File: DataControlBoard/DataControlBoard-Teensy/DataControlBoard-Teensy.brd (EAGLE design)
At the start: 63.5 x 91.4 mm, 11 parts, among them IC1 74LS165D, IC2 74LS165D, J1 RS-Interface, J2 Pwr-Conn, U1 MAX3232, U2 3V3REG

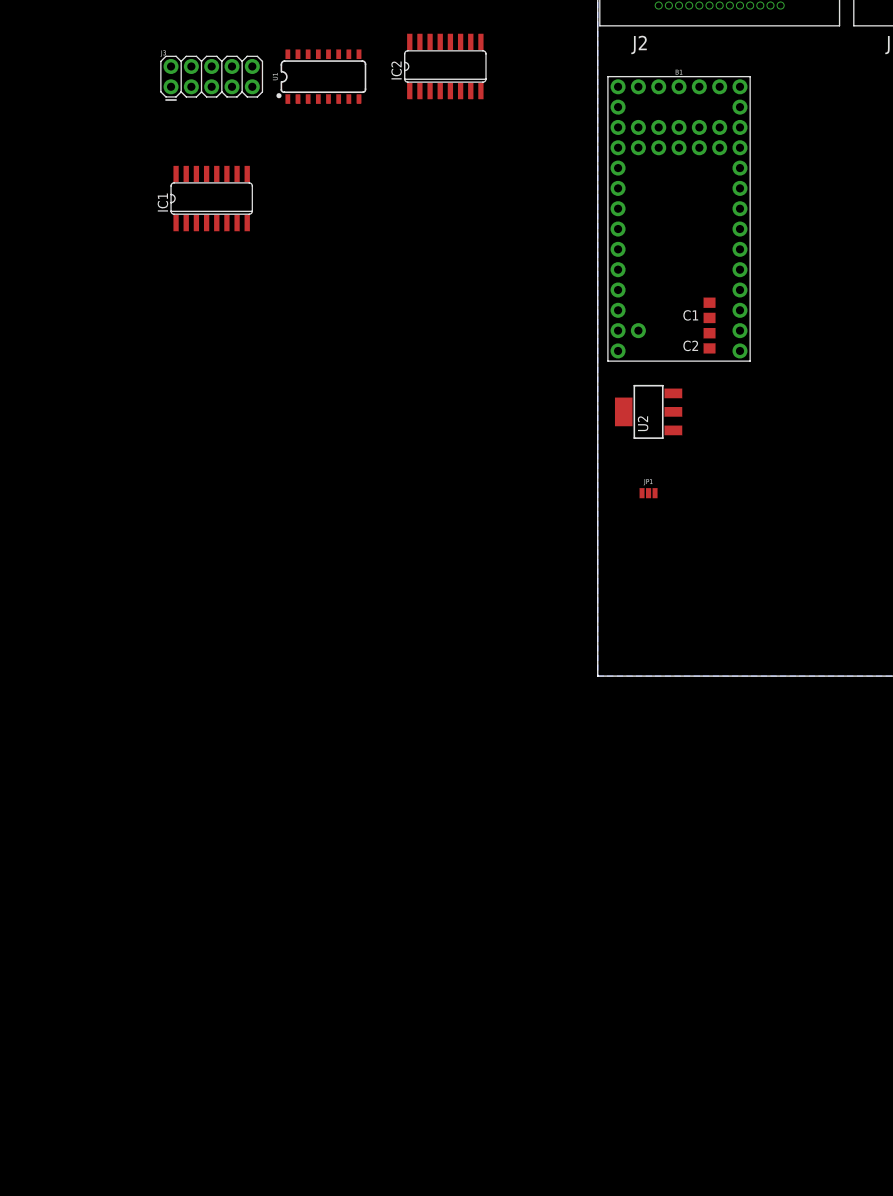
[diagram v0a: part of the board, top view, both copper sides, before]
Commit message: Schematic mostly done. Needs rpi backplane mating header, and a bunch of jumpers
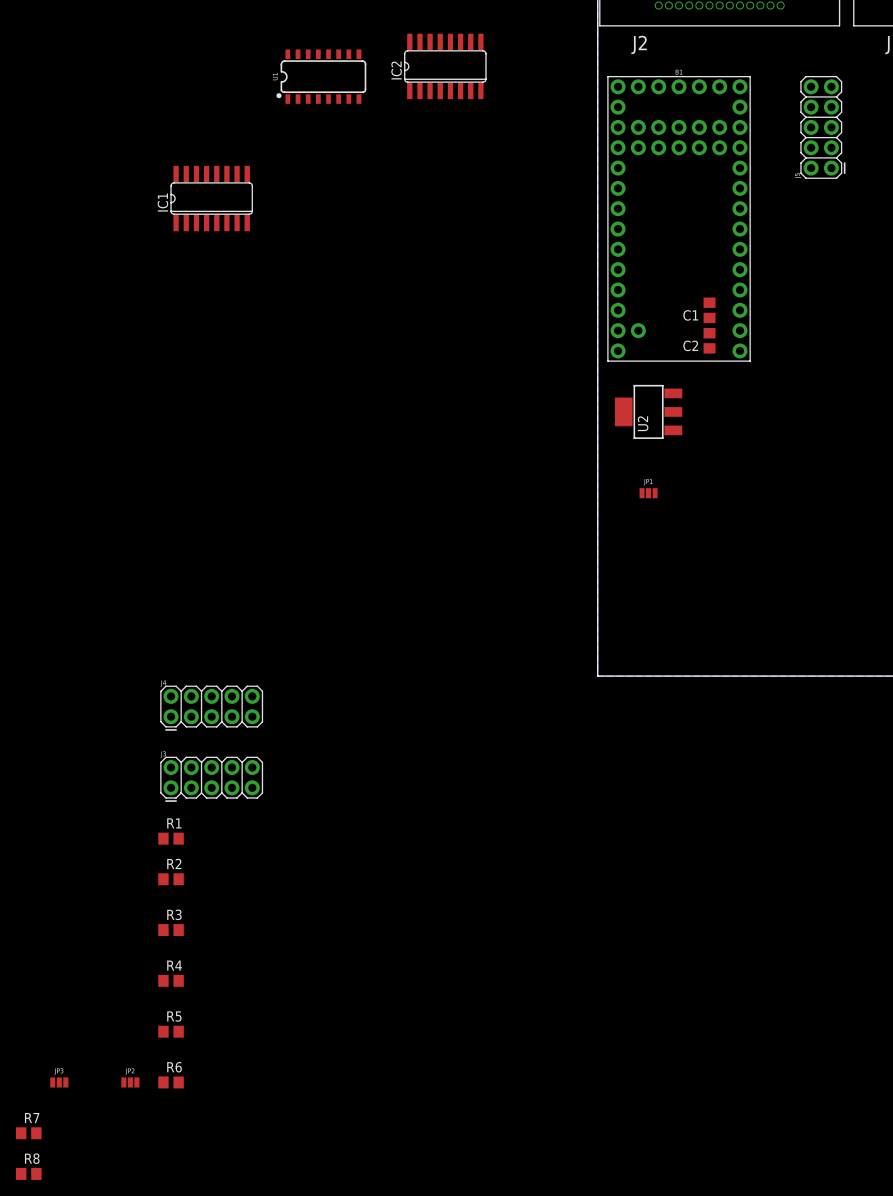
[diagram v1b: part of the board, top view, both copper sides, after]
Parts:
- added J4: Magnet RPi, SparkFun-Connectors:2X5
- added J5: Laser RPi, SparkFun-Connectors:2X5
- added JP2, JP3: JUMPER-SMT_3_NO_NO-SILK, SparkFun-Jumpers:SMT-JUMPER_3_NO_NO-SILK
- added R1, R2, R3, R4, R5, R6: 4.7k, rcl:R0805
- added R7: 10k, rcl:R0805
- added R8: 15k, rcl:R0805
- J3: value (none) -> Static RPi
- moved J3 87.6 mm to (-53.3, -14.0)
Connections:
- net N$4 renamed +5V
- removed net 3.3V: B1.3.3V
- removed net AGND: B1.AGND
- removed net GND1: B1.GND1
- new net LAS-COMM-EN: B1.B32, J5.9
- new net MAG-COMM-EN: B1.B31, J4.9
- new net N$10: J5.8
- new net N$11: J5.10
- new net N$12: B1.3
- new net N$13: J4.2
- new net N$14: J4.4
- new net N$15: J4.6
- new net N$16: J4.8
- new net N$17: J4.10
- new net N$18: J3.5
- new net N$19: J3.7
- new net N$2: J4.5
- new net N$20: B1.4
- new net N$21: J3.2
- new net N$22: J3.4
- new net N$23: J3.6
- new net N$24: J3.8
- new net N$25: J3.10
- new net N$26: B1.5
- new net N$3: J4.7
- new net N$4: J5.5
- new net N$5: J5.7
- new net N$7: J5.2
- new net N$8: J5.4
- new net N$9: J5.6
- new net PDB-STROBE-3V3: B1.2, R7.1, R8.2
- new net PI-SCL: B1.B24, J3.3, J4.3, J5.3, R2.1
- new net PI-SDA: B1.B25, J3.1, J4.1, J5.1, R1.1
- new net SCL0: B1.19, R4.1
- new net SCL1: B1.16, R6.1
- new net SDA0: B1.18, R3.1
- new net SDA1: B1.17, R5.1
- new net STA-COMM-EN: B1.B30, J3.9
- new net UART-TX: B1.8
- net +3V3: now also B1.3.3V, R1.2, R2.2, R3.2, R4.2, R5.2, R6.2
- net GND: now also B1.AGND, B1.GND1, R8.1
- net PDB-STROBE: now also R7.2

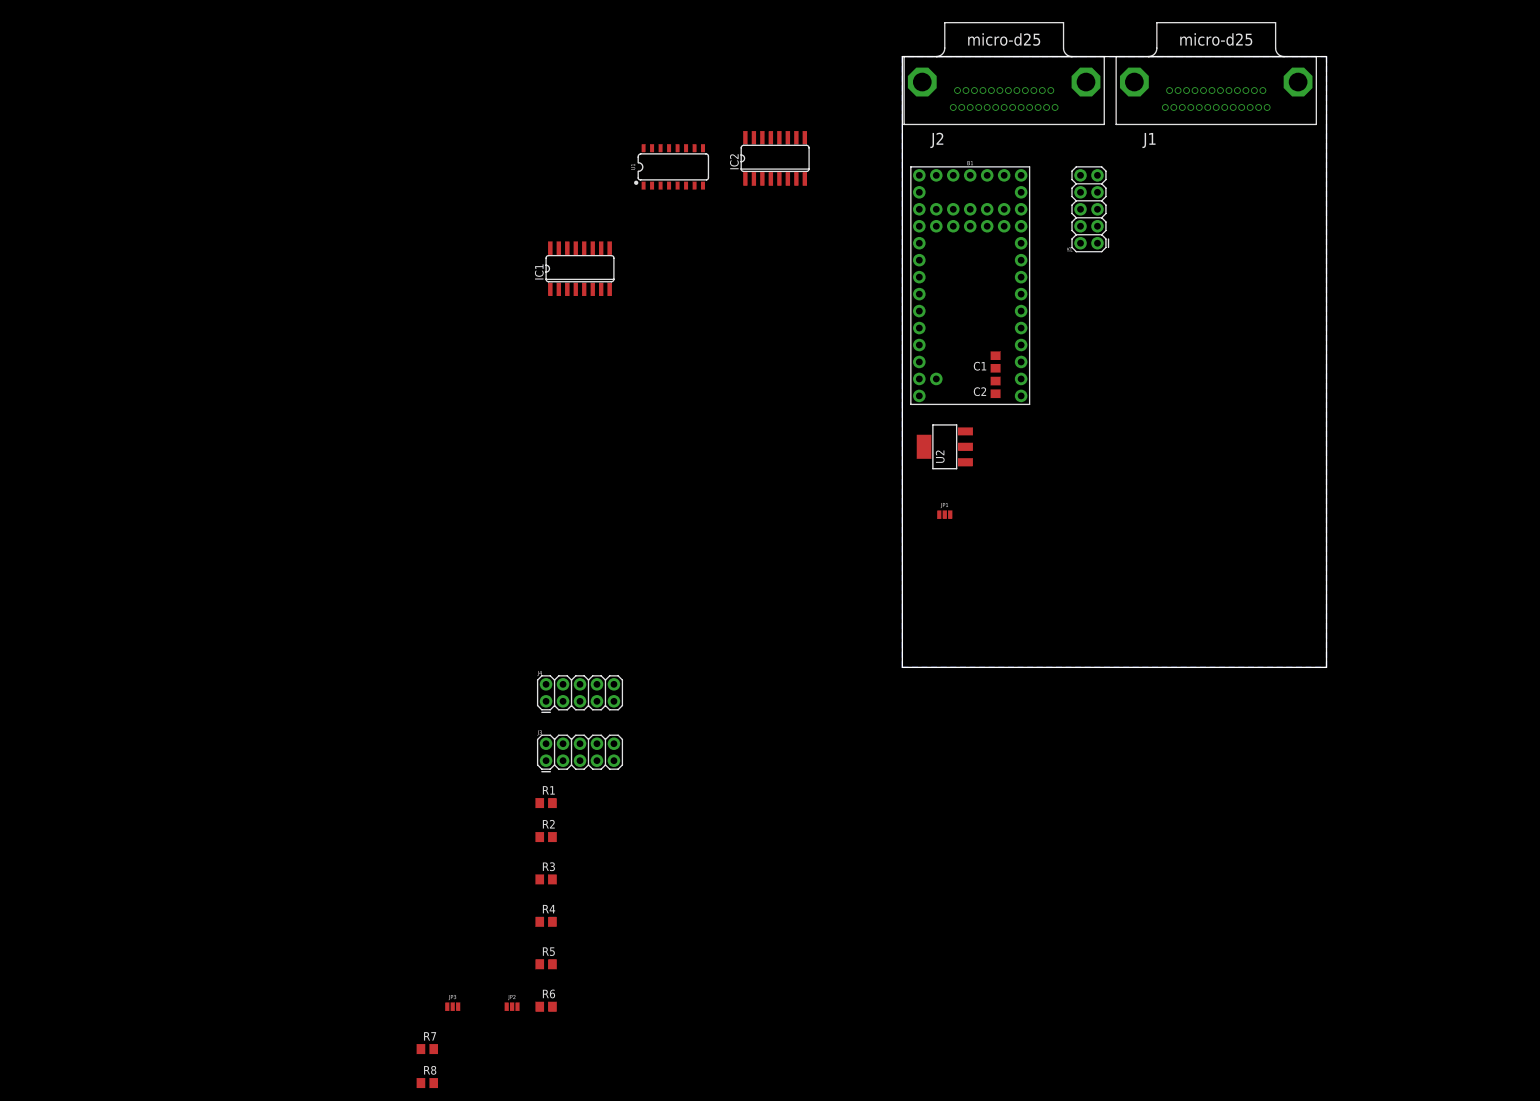
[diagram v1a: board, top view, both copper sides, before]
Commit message: Rearranged DataControl-Teensy
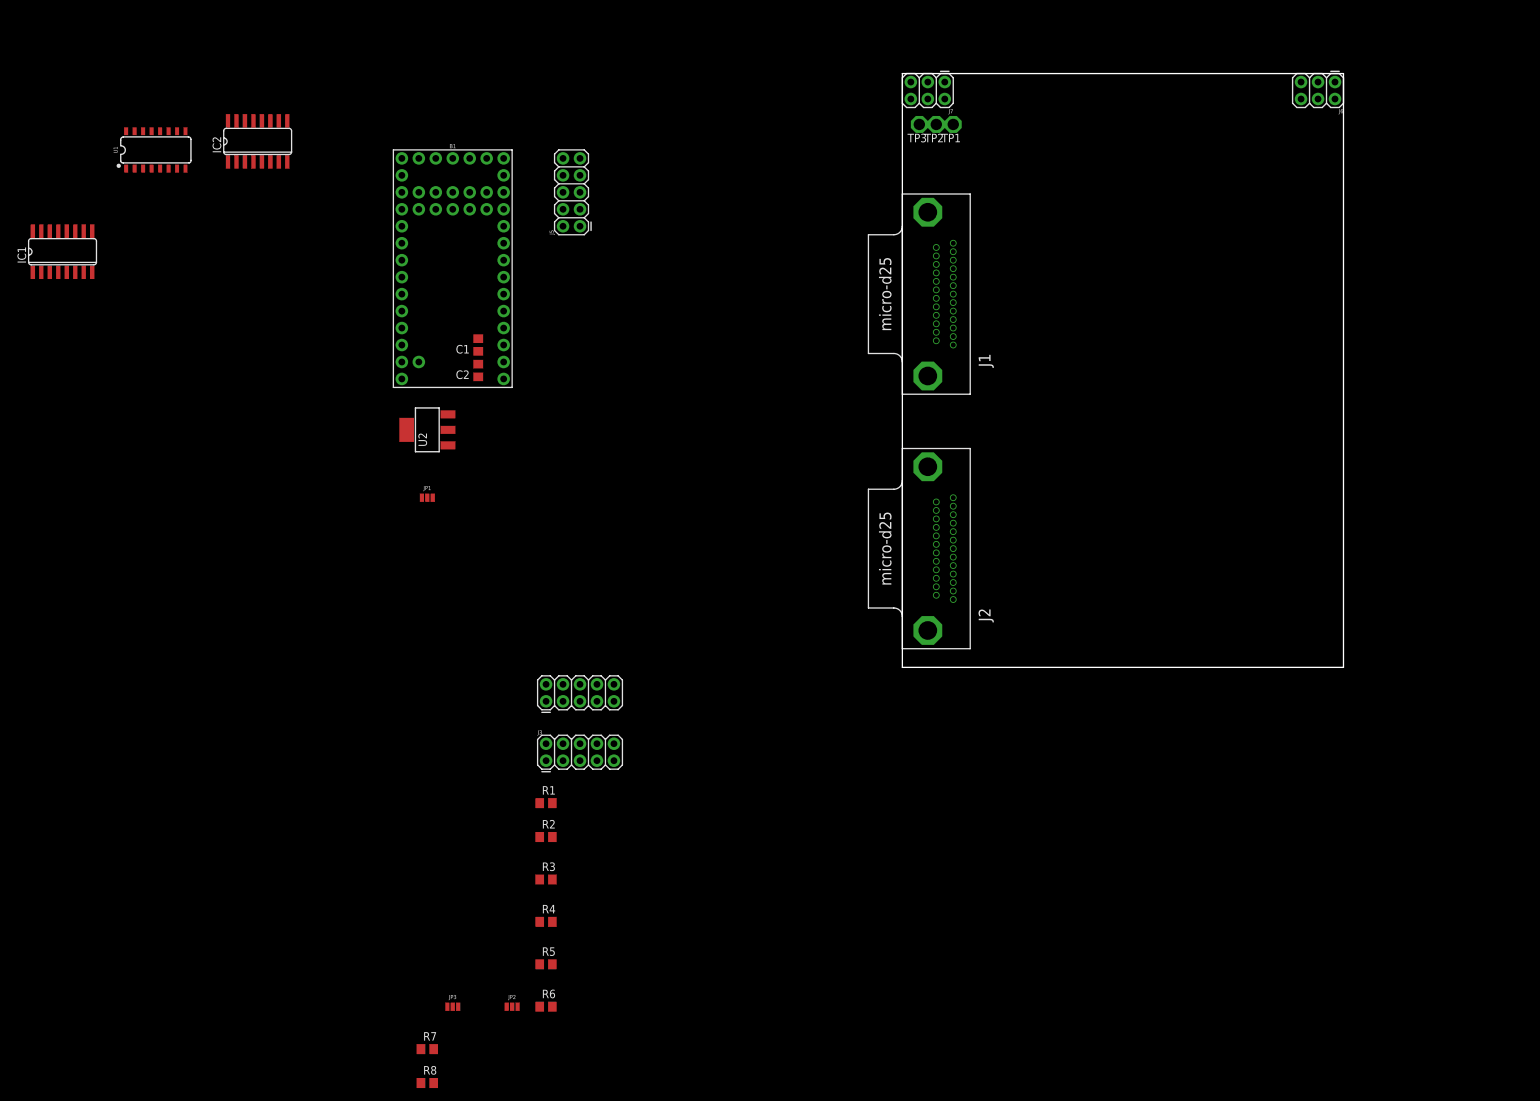
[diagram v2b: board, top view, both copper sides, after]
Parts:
- added J6, J7: (no value), SparkFun-Connectors:2X3
- added TP1, TP2, TP3: TPPAD1-17, testpad:P1-17
- moved B1 77.5 mm to (-67.3, 59.7)
- moved C1 77.5 mm to (-63.5, 48.3)
- moved C2 77.5 mm to (-63.5, 44.5)
- moved IC1 77.5 mm to (-125.7, 62.2)
- moved IC2 77.5 mm to (-96.5, 78.7)
- moved J5 77.5 mm to (-48.3, 66.0)
- moved JP1 77.5 mm to (-71.1, 25.4)
- moved U1 77.5 mm to (-111.8, 77.5)
- moved U2 77.5 mm to (-71.1, 35.6)
- moved J2 66.5 mm to (7.62, 17.8), turned to 90 degrees
- moved J1 48.3 mm to (7.62, 55.9), turned to 90 degrees
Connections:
- new net N$27: J7.4, TP2.TP
- new net N$28: J7.6, TP3.TP
- new net N$6: J7.2, TP1.TP
- net 5V-DIG-CAM: now also J6.3
- net 5V-DIG-LASER: now also J6.4
- net 5V-DIG-MAG: now also J6.5
- net 5V-DIG-STA: now also J6.2
- net 5V-DIG-TX: now also J6.1
- net GND: now also J6.6, J7.1, J7.3, J7.5
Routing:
- removed copper zone on layer 16, net GND
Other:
- board size 63.5 x 91.4 mm -> 66 x 88.9 mm

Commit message: Added jumper selection for sda/scl and wired rs232 converter
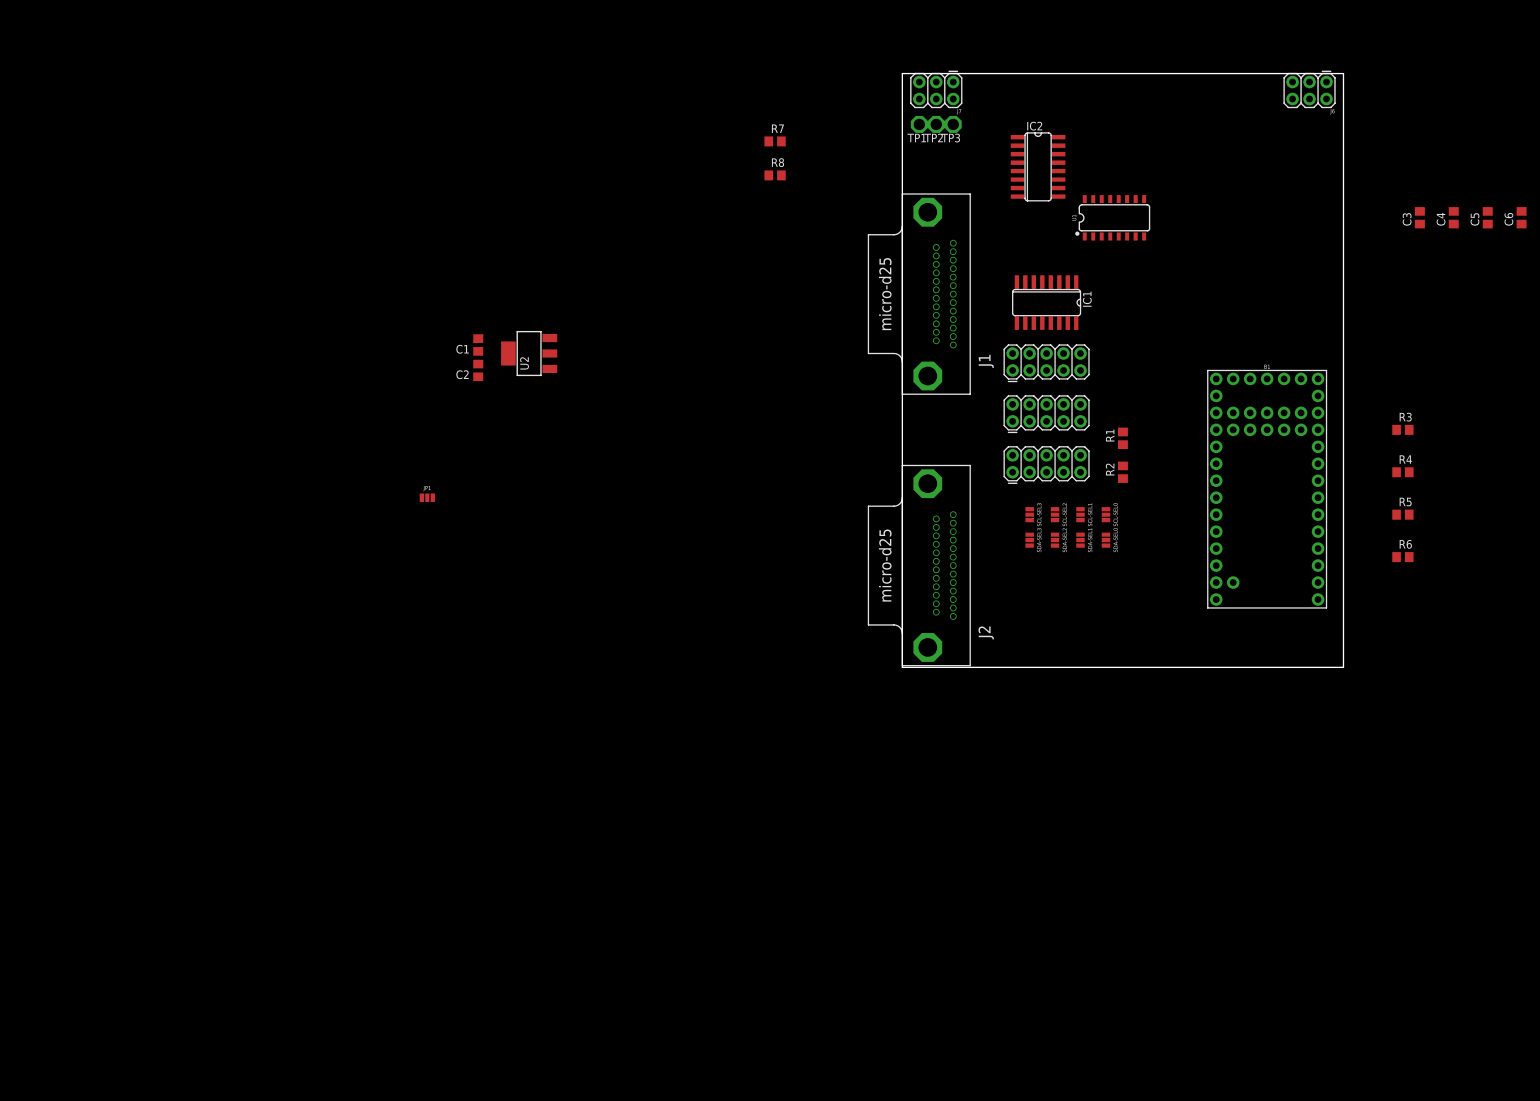
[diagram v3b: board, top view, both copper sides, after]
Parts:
- removed JP2, JP3: JUMPER-SMT_3_NO_NO-SILK, SparkFun-Jumpers:SMT-JUMPER_3_NO_NO-SILK
- added C3, C4, C5, C6: 0.1uF, rcl:C0805
- added SCL-SEL0, SCL-SEL1, SCL-SEL2, SCL-SEL3, SDA-SEL0, SDA-SEL1, SDA-SEL2, SDA-SEL3: JUMPER-SMT_3_NO_NO-SILK, SparkFun-Jumpers:SMT-JUMPER_3_NO_NO-SILK
- J5: value Laser RPi -> Boom Cam RPi
- moved IC1 147.5 mm to (21.6, 54.6), turned to 180 degrees
- moved R7 145.5 mm to (-19.1, 78.7)
- moved R8 145.5 mm to (-19.1, 73.7)
- moved R3 144.9 mm to (74.9, 35.6)
- moved R4 144.9 mm to (74.9, 29.2)
- moved R5 144.9 mm to (74.9, 22.9)
- moved R6 144.9 mm to (74.9, 16.5)
- moved U1 143.9 mm to (31.8, 67.3)
- moved B1 126.3 mm to (54.6, 26.7)
- moved IC2 116.9 mm to (20.3, 74.9), turned to 270 degrees
- moved R1 102.2 mm to (33.0, 34.3), turned to 90 degrees
- moved R2 102.2 mm to (33.0, 29.2), turned to 90 degrees
- moved J3 82.1 mm to (16.5, 29.2)
- moved J4 81.5 mm to (16.5, 36.8)
- moved J5 68.3 mm to (16.5, 44.5), turned to 0 degrees
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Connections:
- removed net N$1: IC1.2, IC2.2
- removed net N$12: B1.3
- removed net N$20: B1.4
- removed net N$26: B1.5
- new net N$32: C5.1, U1.2
- new net N$33: C6.1, U1.6
- new net N$34: C3.1, U1.1
- new net N$35: C3.2, U1.3
- new net N$36: C4.1, U1.4
- new net N$37: C4.2, U1.5
- new net SHIFT-CLK: B1.4, IC1.2, IC2.2
- net +3V3: now also U1.16
- net BOOM-I2C-SCL: now also SCL-SEL3.2
- net BOOM-I2C-SDA: now also SDA-SEL3.2
- net GND: now also C5.2, C6.2, U1.15
- net LASER-I2C-SCL: now also SCL-SEL0.2
- net LASER-I2C-SDA: now also SDA-SEL0.2
- net MAGNET-I2C-SCL: now also SCL-SEL2.2
- net MAGNET-I2C-SDA: now also SDA-SEL2.2
- net N$28: now also TP1.TP; no longer TP3.TP
- net N$6: now also TP3.TP; no longer TP1.TP
- net RS232-DATA: now also U1.14
- net SCL0: now also SCL-SEL0.3, SCL-SEL1.3, SCL-SEL2.3, SCL-SEL3.3
- net SCL1: now also SCL-SEL0.1, SCL-SEL1.1, SCL-SEL2.1, SCL-SEL3.1
- net SDA0: now also SDA-SEL0.3, SDA-SEL1.3, SDA-SEL2.3, SDA-SEL3.3
- net SDA1: now also SDA-SEL0.1, SDA-SEL1.1, SDA-SEL2.1, SDA-SEL3.1
- net SHIFT-IN: now also B1.3
- net SHIFT-LAT: now also B1.5
- net STATIC-I2C-SCL: now also SCL-SEL1.2
- net STATIC-I2C-SDA: now also SDA-SEL1.2
- net UART-TX: now also U1.11
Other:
- board text added: "Note: Connector sizes might be off. Stay 100 mil away from connector housing front to back"

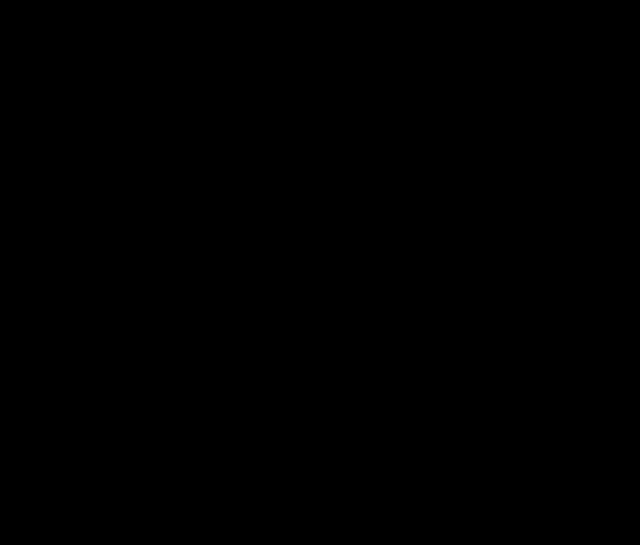
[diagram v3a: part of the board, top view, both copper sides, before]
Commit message: Data control schem ready for double-check
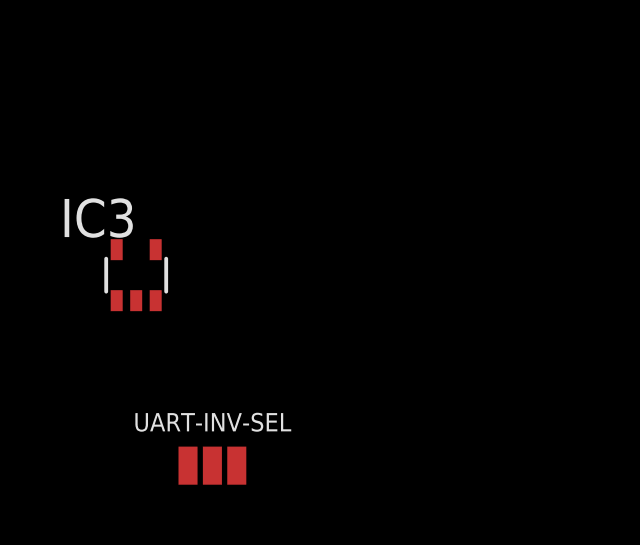
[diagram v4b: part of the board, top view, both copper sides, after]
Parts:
- added IC3: 74AHC1G04DCK, 74xx-little-de:SC70-5
- added UART-INV-SEL: JUMPER-SMT_3_NO_NO-SILK, SparkFun-Jumpers:SMT-JUMPER_3_NO_NO-SILK
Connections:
- new net N$20: U1.11, UART-INV-SEL.2
- new net UART-TX-INV: IC3.4, UART-INV-SEL.1
- net +3V3: now also IC3.5
- net GND: now also IC3.3
- net UART-TX: now also IC3.2, UART-INV-SEL.3; no longer U1.11
